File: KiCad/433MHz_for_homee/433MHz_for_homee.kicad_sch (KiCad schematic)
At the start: 9 parts, among them Q1 BC547, Q2 BC547, SW1 SysMode, U1 ESP32-C3_SUPERMINI_TH, U2 4x Level Converter Module (3.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

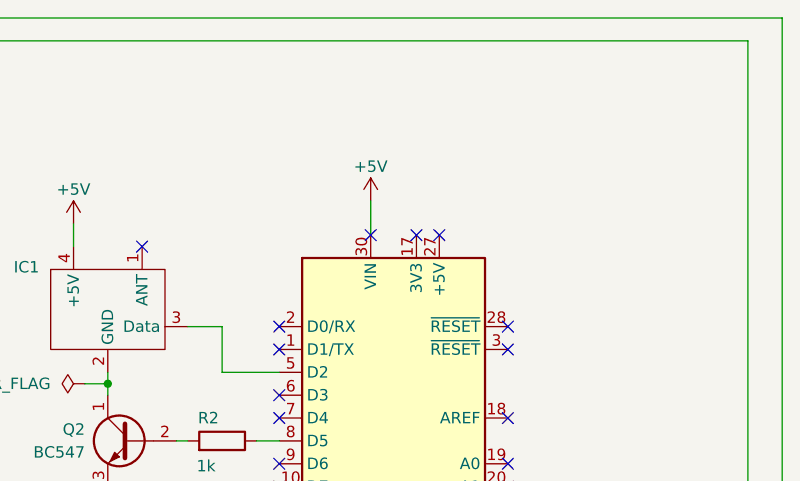
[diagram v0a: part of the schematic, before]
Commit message: fixed a bug in the PCB
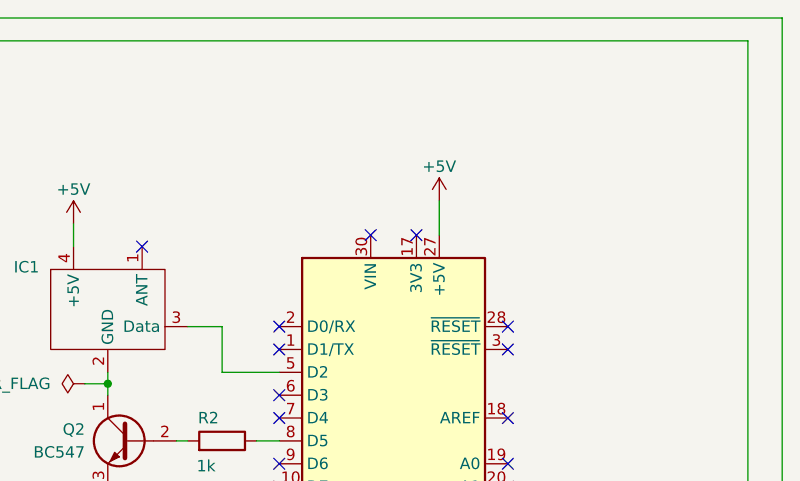
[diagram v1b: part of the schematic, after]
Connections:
- net +5V: now also A1.27 (+5V); no longer A1.30 (VIN)
- no-connect marks 38 -> 37
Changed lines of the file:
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@@
-	)
-	(no_connect
-		(at 234.95 48.26)
 	)
 	(no_connect
@@
 	(wire
 		(pts
-			(xy 227.33 44.45) (xy 227.33 48.26)
-		)
-		(stroke
-			(width 0)
-			(type default)
-		)
-	)
-	(wire
-		(pts
 			(xy 46.99 68.58) (xy 30.48 68.58)
 		)
@@
 		(pts
 			(xy 208.28 118.11) (xy 223.52 118.11)
+		)
+		(stroke
+			(width 0)
+			(type default)
+		)
+	)
+	(wire
+		(pts
+			(xy 234.95 44.45) (xy 234.95 48.26)
 		)
 		(stroke
@@
 	(symbol
 		(lib_id "power:+5V")
-		(at 227.33 44.45 0)
+		(at 234.95 44.45 0)
 		(unit 1)
 		(exclude_from_sim no)
@@
 		(dnp no)
 		(property "Reference" "#PWR08"
-			(at 227.33 48.26 0)
+			(at 234.95 48.26 0)
 			(effects
 				(font
@@
 		)
 		(property "Value" "+5V"
-			(at 227.33 40.64 0)
+			(at 234.95 40.64 0)
 			(effects
 				(font
@@
 		)
 		(property "Footprint" ""
-			(at 227.33 44.45 0)
+			(at 234.95 44.45 0)
 			(effects
 				(font
@@
 		)
 		(property "Datasheet" ""
-			(at 227.33 44.45 0)
+			(at 234.95 44.45 0)
 			(effects
 				(font
@@
 		)
 		(property "Description" "Power symbol creates a global label with name \"+5V\""
-			(at 227.33 44.45 0)
-			(effects
-				(font
+			(at 234.95 44.45 0)
+			(effects
+				(font

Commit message: User manual updated
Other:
- company: (none) -> Andreas Schmack (C)
- title: (none) -> EV1527 433MHz for homee
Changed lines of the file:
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@@
 	(generator_version "9.0")
 	(paper "A4")
+	(title_block
+		(title "EV1527 433MHz for homee")
+		(date "2025-07-26")
+		(rev "1.1")
+		(company "Andreas Schmack (C)")
+	)
 	(junction
 		(at 229.87 100.33)
